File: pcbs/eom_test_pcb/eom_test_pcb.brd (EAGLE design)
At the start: 160 x 48 mm, 72 parts

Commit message: board in finished state, sending to PCBWay
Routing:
- added copper zone on layer 15, net GND
- added copper zone on layer 16, net GND
- added copper zone on layer 2, net GND
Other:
- board text added: "1 2 4 6 8 3 5 7 9"
- board text added: "8 6 4 2 1 3 5 7 9"

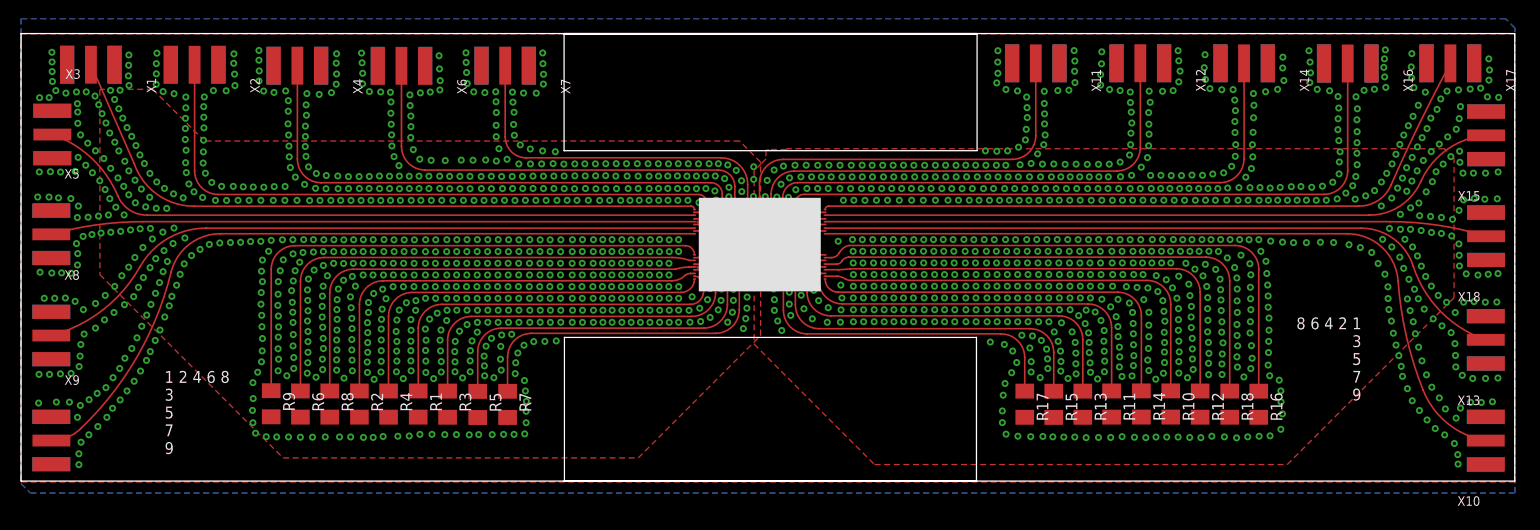
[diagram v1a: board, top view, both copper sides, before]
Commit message: Fixed board to have correct layer thickness
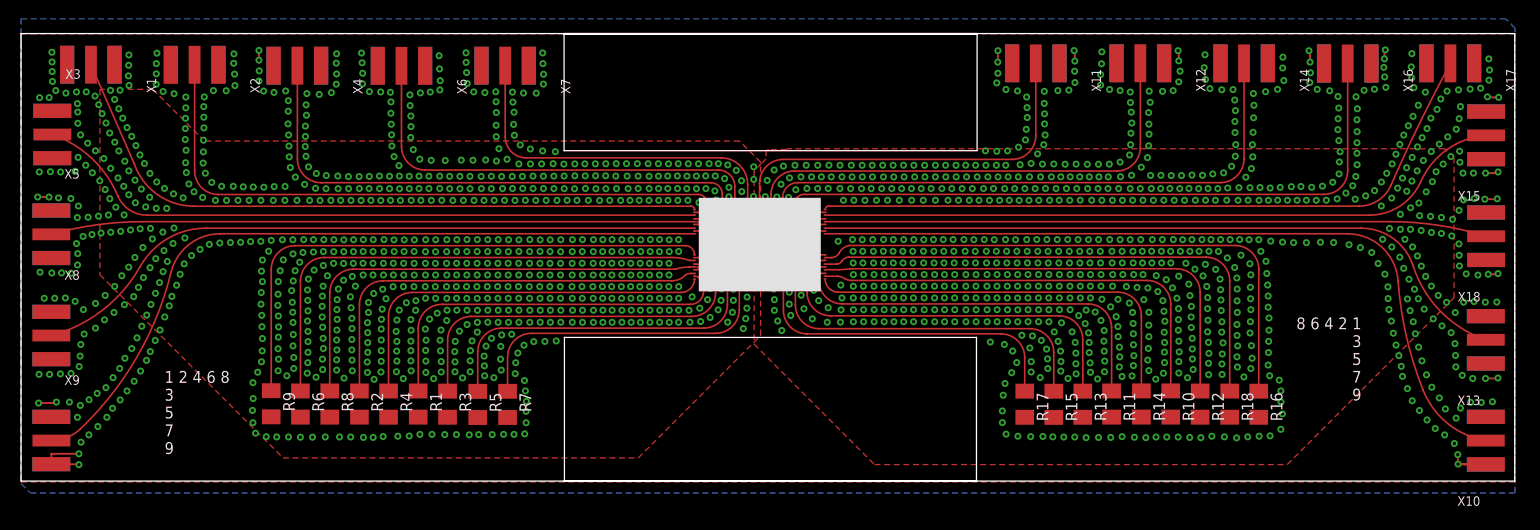
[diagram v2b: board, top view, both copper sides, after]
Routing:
- net GND: track 0.00 -> 31.0 mm

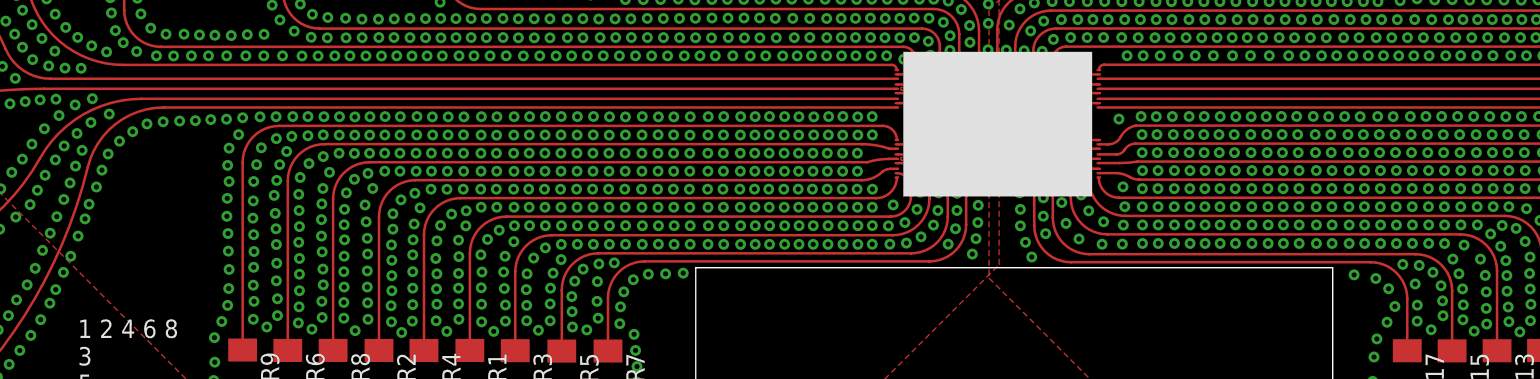
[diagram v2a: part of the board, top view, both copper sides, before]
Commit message: Push before mitering
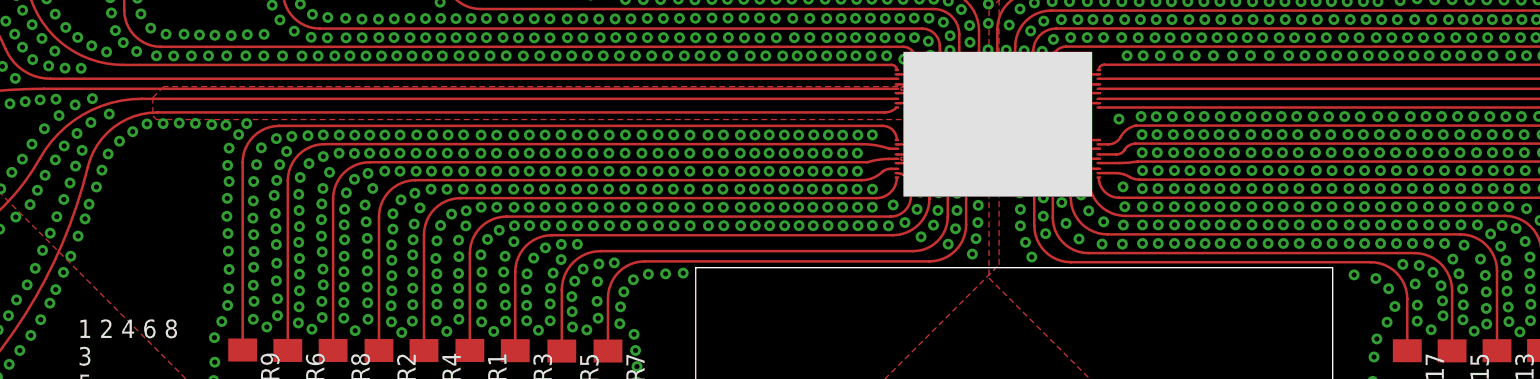
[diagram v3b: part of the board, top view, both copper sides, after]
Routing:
- net GND: vias 1857 -> 1796

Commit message: Push after sending to PCBWay in this state
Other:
- board size 160 x 48 mm -> 160.3 x 47.9 mm
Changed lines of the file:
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@@
 <setting verticaltext="up"/>
 </settings>
-<grid distance="100" unitdist="mil" unit="mil" style="lines" multiple="1" display="no" altdistance="0.001" altunitdist="mil" altunit="mil"/>
+<grid distance="10" unitdist="mil" unit="mil" style="lines" multiple="1" display="no" altdistance="0.001" altunitdist="mil" altunit="mil"/>
 <layers>
 <layer number="1" name="Top" color="4" fill="1" visible="yes" active="yes"/>
@@
 <board>
 <plain>
-<wire x1="0" y1="52.07" x2="160" y2="52.07" width="0" layer="20"/>
+<wire x1="0" y1="52.07" x2="58.109459375" y2="52.07" width="0" layer="20"/>
+<wire x1="58.109459375" y1="52.07" x2="58.5160625" y2="52.22263125" width="0" layer="20"/>
+<wire x1="58.5160625" y1="52.22263125" x2="58.5166" y2="65.291534375" width="0" layer="20"/>
+<wire x1="58.5166" y1="65.291534375" x2="58.8541125" y2="66.4930875" width="0" layer="20"/>
+<wire x1="58.8541125" y1="66.4930875" x2="101.2459" y2="66.52275" width="0" layer="20"/>
+<wire x1="101.2459" y1="66.52275" x2="102.17505625" y2="65.502840625" width="0" layer="20"/>
+<wire x1="102.17505625" y1="65.502840625" x2="102.17505625" y2="52.21094375" width="0" layer="20"/>
+<wire x1="102.17505625" y1="52.21094375" x2="102.320903125" y2="52.065096875" width="0" layer="20"/>
+<wire x1="102.320903125" y1="52.065096875" x2="160" y2="52.07" width="0" layer="20"/>
 <wire x1="160" y1="52.07" x2="160" y2="100" width="0" layer="20"/>
-<wire x1="160" y1="100" x2="0" y2="100" width="0" layer="20"/>
-<wire x1="0" y1="100" x2="0" y2="52.07" width="0" layer="20"/>
+<wire x1="160" y1="100" x2="102.4691875" y2="100.0101875" width="0" layer="20"/>
+<wire x1="102.4691875" y1="100.0101875" x2="102.261415625" y2="99.802415625" width="0" layer="20"/>
+<wire x1="102.261415625" y1="99.802415625" x2="102.07911875" y2="88.90134375" width="0" layer="20"/>
+<wire x1="102.07911875" y1="88.90134375" x2="101.551584375" y2="88.197640625" width="0" layer="20"/>
+<wire x1="101.551584375" y1="88.197640625" x2="58.65636875" y2="88.223196875" width="0" layer="20"/>
+<wire x1="58.65636875" y1="88.223196875" x2="58.1612" y2="88.9323375" width="0" layer="20"/>
+<wire x1="58.1612" y1="88.9323375" x2="58.167496875" y2="99.7101125" width="0" layer="20"/>
+<wire x1="58.167496875" y1="99.7101125" x2="57.90395" y2="100" width="0" layer="20"/>
+<wire x1="57.90395" y1="100" x2="-0.254" y2="100" width="0" layer="20"/>
+<wire x1="-0.254" y1="100" x2="0" y2="52.07" width="0" layer="20"/>
 <rectangle x1="72.59" y1="72.39" x2="85.671" y2="82.423" layer="21"/>
-<dimension x1="72.39" y1="82.423" x2="72.39" y2="81.153" x3="70.8406" y3="81.788" textsize="0.254" layer="25" width="0.0254" unit="mil" precision="0"/>
-<dimension x1="72.39" y1="82.423" x2="72.39" y2="81.153" x3="69.85" y3="81.788" textsize="0.254" layer="25" width="0.0254" unit="mic" precision="0"/>
-<dimension x1="85.671" y1="82.423" x2="85.67" y2="81.153" x3="87.122196875" y3="81.78685625" textsize="0.254" layer="25" width="0.0254" unit="mil" precision="1"/>
-<dimension x1="85.671" y1="82.423" x2="86.1314" y2="82.423" x3="85.9012" y3="81.153" textsize="0.254" layer="25" width="0.0254" unit="mil" precision="1"/>
-<rectangle x1="58.17" y1="87.46" x2="102.4" y2="99.99" layer="46"/>
-<rectangle x1="58.2" y1="52.06" x2="102.34" y2="67.46" layer="46"/>
-<rectangle x1="58.17" y1="99.99" x2="102.4" y2="100.01" layer="46"/>
 <rectangle x1="71.597775" y1="72.45223125" x2="72.58964375" y2="82.3572125" layer="29"/>
 <rectangle x1="85.68486875" y1="72.4573125" x2="86.6767375" y2="82.36229375" layer="29"/>
@@
             7
             9</text>
+<rectangle x1="70.538034375" y1="72.451975" x2="71.597821875" y2="82.35688125" layer="29"/>
+<rectangle x1="86.676075" y1="72.457234375" x2="87.7358625" y2="82.362140625" layer="29"/>
 </plain>
 <attributes>
@@
 <param name="mdViaViaSameLayer" value="6mil"/>
 <param name="mnLayersViaInSmd" value="2"/>
-<param name="mdCopperDimension" value="40mil"/>
+<param name="mdCopperDimension" value="30mil"/>
 <param name="mdDrill" value="6mil"/>
 <param name="mdSmdStop" value="0mil"/>
@@
 <vertex x="8.448040625" y="94.015559375"/>
 <vertex x="8.448040625" y="74.170540625"/>
-<vertex x="28.069540625" y="54.549040625"/>
-<vertex x="66.11111875" y="54.549040625"/>
+<vertex x="16.24208125" y="66.3765"/>
+<vertex x="19.61515" y="55.833009375"/>
+<vertex x="21.004478125" y="54.44368125"/>
+<vertex x="53.8115" y="54.44368125"/>
+<vertex x="56.332703125" y="56.964884375"/>
+<vertex x="56.332703125" y="64.26408125"/>
+<vertex x="58.445121875" y="66.3765"/>
+<vertex x="77.938578125" y="66.3765"/>
 <vertex x="79.220059375" y="67.65798125"/>
-<vertex x="79.220059375" y="86.233"/>
-<vertex x="76.959459375" y="88.4936"/>
+<vertex x="79.220059375" y="88.4936"/>
 <vertex x="19.65198125" y="88.4936"/>
 <vertex x="14.112240625" y="94.033340625"/>
@@
 <via x="108.8898" y="87.11691875" extent="1-16" drill="0.35" diameter="0.55"/>
 <polygon width="0.0762" layer="1" spacing="0.254" isolate="0.1524" orphans="yes" thermals="no">
-<vertex x="79.796640625" y="87.5157"/>
-<vertex x="79.796640625" y="86.580978125"/>
-<vertex x="79.31658125" y="86.10091875"/>
-<vertex x="78.5241" y="85.3084375"/>
-<vertex x="78.5241" y="66.735959375"/>
-<vertex x="91.42221875" y="53.837840625"/>
-<vertex x="104.764840625" y="53.837840625"/>
-<vertex x="135.625840625" y="53.837840625"/>
+<vertex x="78.1661625" y="88.524790625"/>
+<vertex x="78.1661625" y="67.67205"/>
+<vertex x="78.812946875" y="67.025265625"/>
+<vertex x="101.382553125" y="67.025265625"/>
+<vertex x="104.14" y="64.26781875"/>
+<vertex x="104.14" y="56.95124375"/>
+<vertex x="107.074765625" y="54.016478125"/>
+<vertex x="137.55893125" y="54.016478125"/>
+<vertex x="139.5595375" y="56.017084375"/>
+<vertex x="148.813265625" y="67.025265625"/>
 <vertex x="153.49728125" y="71.70928125"/>
 <vertex x="153.49728125" y="86.657178125"/>
-<vertex x="152.486359375" y="87.6681"/>
-<vertex x="82.0674" y="87.6681"/>
-<vertex x="81.98358125" y="87.58428125"/>
-<vertex x="80.1116" y="87.58428125"/>
-<vertex x="80.058259375" y="87.530940625"/>
-<vertex x="79.91348125" y="87.530940625"/>
-<vertex x="79.905859375" y="87.52331875"/>
-<vertex x="79.80171875" y="87.52331875"/>
-<vertex x="79.796640625" y="87.518240625"/>
+<vertex x="151.62966875" y="88.524790625"/>
 </polygon>
 <via x="110.096046875" y="69.134225" extent="1-16" drill="0.35" diameter="0.55"/>
